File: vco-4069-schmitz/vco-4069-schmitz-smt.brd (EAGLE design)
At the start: 58.4 x 36.8 mm, 46 parts, among them IC1 4069N, J1 22k pot (fp), J2 22k pot (fp), Q1 BC560, Q2 BC550B, Q3 BC550B

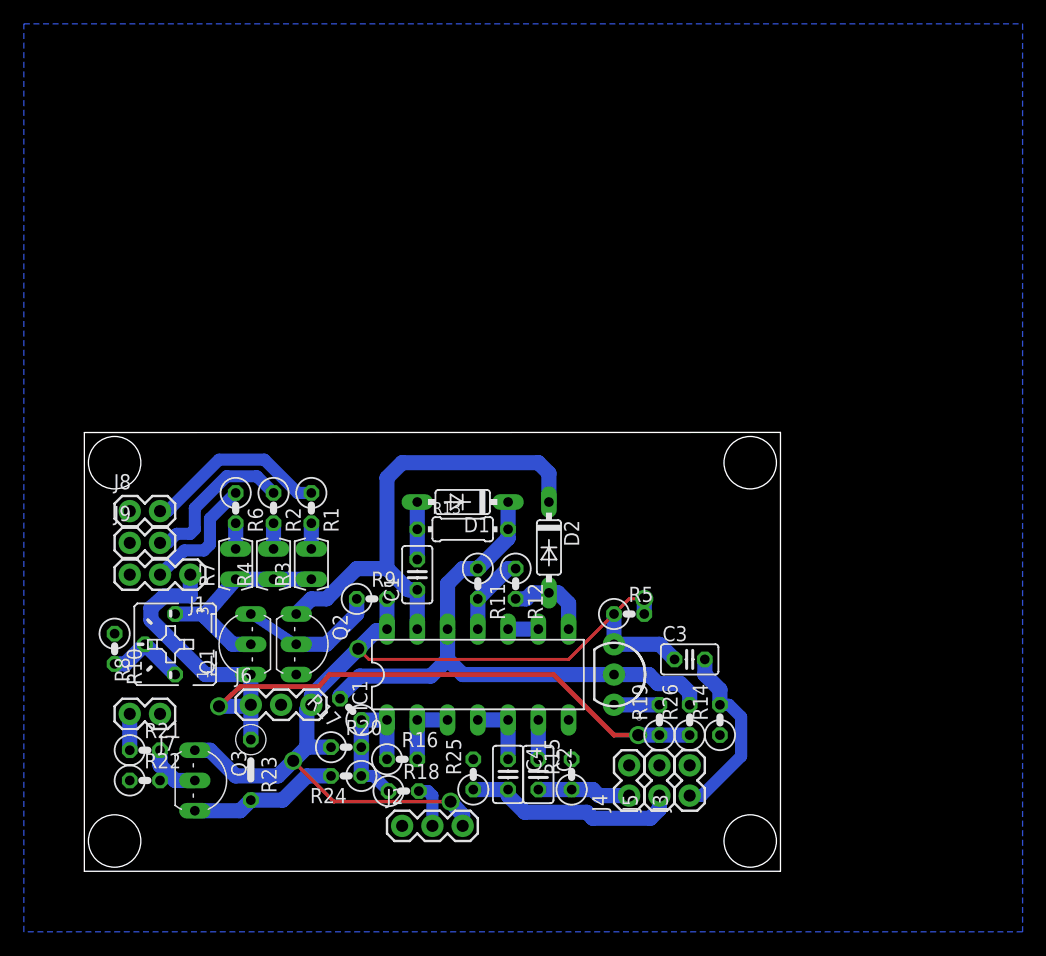
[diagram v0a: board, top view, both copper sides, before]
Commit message: through-hole 4069 vco
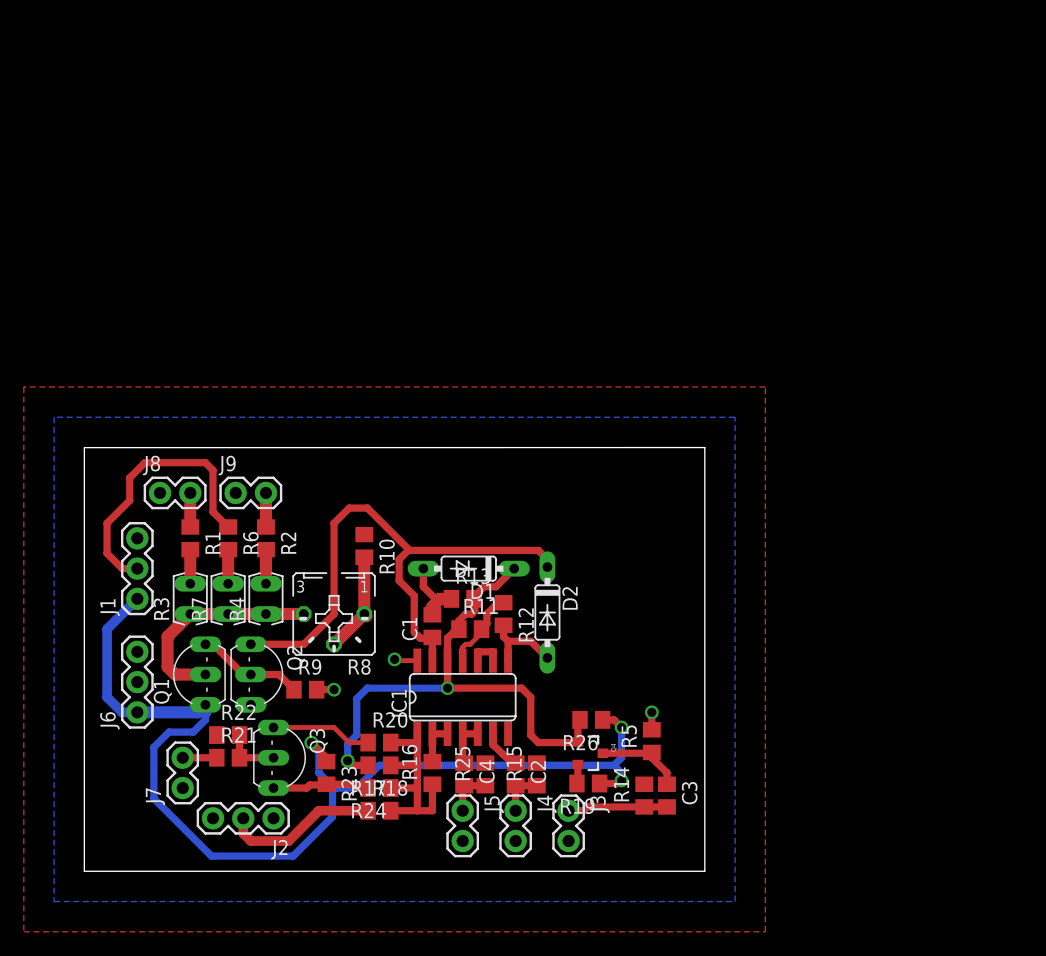
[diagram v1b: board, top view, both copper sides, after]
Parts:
- C1, C2, C3, C4: device resistor:C025-025X050 -> resistor:C0805
- IC1: value 4069N -> 4069D; device 40xx:DIL14 -> 40xx:SO14
- Q4: device SparkFun-DiscreteSemi:TO-92-AMMO -> SparkFun-DiscreteSemi:SOT23-3
- R1, R10, R11, R12, R14, R15, R16, R17, R18, R19, R2, R20, R21, R22, R25, R5, R6, R9: device resistor:0207/2V -> resistor:R0805
- R13: device resistor:0204/7 -> resistor:R0805
- R23: device resistor:0207/5V -> resistor:R0805
- R24: value 100k -> 10k; device resistor:0207/2V -> resistor:R0805
- R26: value 33k -> 3.3k; device resistor:0207/2V -> resistor:R0805
- moved R10 22.7 mm to (23.5, 27.3)
- moved J5 16.6 mm to (31.8, 5.08), turned to 270 degrees
- moved R8 13.6 mm to (21.0, 21.6), turned to 180 degrees
- moved C3 11.6 mm to (48.9, 6.35), turned to 270 degrees
- moved R5 10.8 mm to (47.6, 10.9), turned to 90 degrees
- moved J2 10.8 mm to (15.9, 4.45), turned to 180 degrees
- moved R3 10.6 mm to (8.89, 22.9)
- moved R1 10.5 mm to (8.89, 27.9)
- moved J3 10.2 mm to (40.6, 5.08), turned to 270 degrees
- moved J9 9.83 mm to (12.7, 31.8)
- moved J4 9.61 mm to (36.2, 5.08), turned to 270 degrees
- moved J6 9.55 mm to (4.45, 13.3), turned to 90 degrees
- moved R9 9.45 mm to (18.5, 15.2)
- moved R14 8.98 mm to (47.0, 6.35)
- moved R26 8.25 mm to (42.5, 12.7), turned to 180 degrees
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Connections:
- net GND: now also R14.2; no longer R14.1
- net N$14: now also Q4.2; no longer Q4.3
- net N$17: now also R18.2; no longer R18.1
- net N$18: now also R18.1; no longer R18.2
- net N$23: now also Q4.3; no longer Q4.1
- net N$25: now also Q4.1; no longer Q4.2
- net SAW: now also R14.1; no longer R14.2
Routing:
- net +12V: track 73.8 -> 13.3 mm, vias 4 -> 3
- net -12V: track 67.6 -> 89.8 mm, vias 2 -> 3
- net FPULSE: track 18.4 -> 3.93 mm
- net N$1: track 10.5 -> 23.3 mm
- net N$22: track 15.6 -> 2.86 mm
- net CV2: track 13.5 -> 2.86 mm
- net N$18: track 3.84 -> 13.1 mm
- net N$8: track 40.3 -> 48.0 mm
- net SAW: track 15.5 -> 8.39 mm
- net N$17: track 13.0 -> 18.8 mm
- net N$5: track 12.6 -> 8.21 mm
- net PULSE: track 7.83 -> 3.88 mm
- net N$25: track 49.1 -> 45.5 mm, vias 0 -> 2
- net N$6: track 12.0 -> 9.01 mm
- net N$9: track 5.84 -> 3.60 mm
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- added copper zone on layer 16, net +12V
- added copper zone on layer 1, net GND
- removed copper zone on layer 16, net GND
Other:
- board size 58.4 x 36.8 mm -> 52.1 x 35.6 mm
